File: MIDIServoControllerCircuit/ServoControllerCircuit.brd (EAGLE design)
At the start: 59 x 66 mm, 26 parts, among them Q1 20MHz, T1 2N3904, X1 SIGNAL-PWR-GND, X2 SIGNAL-PWR-GND

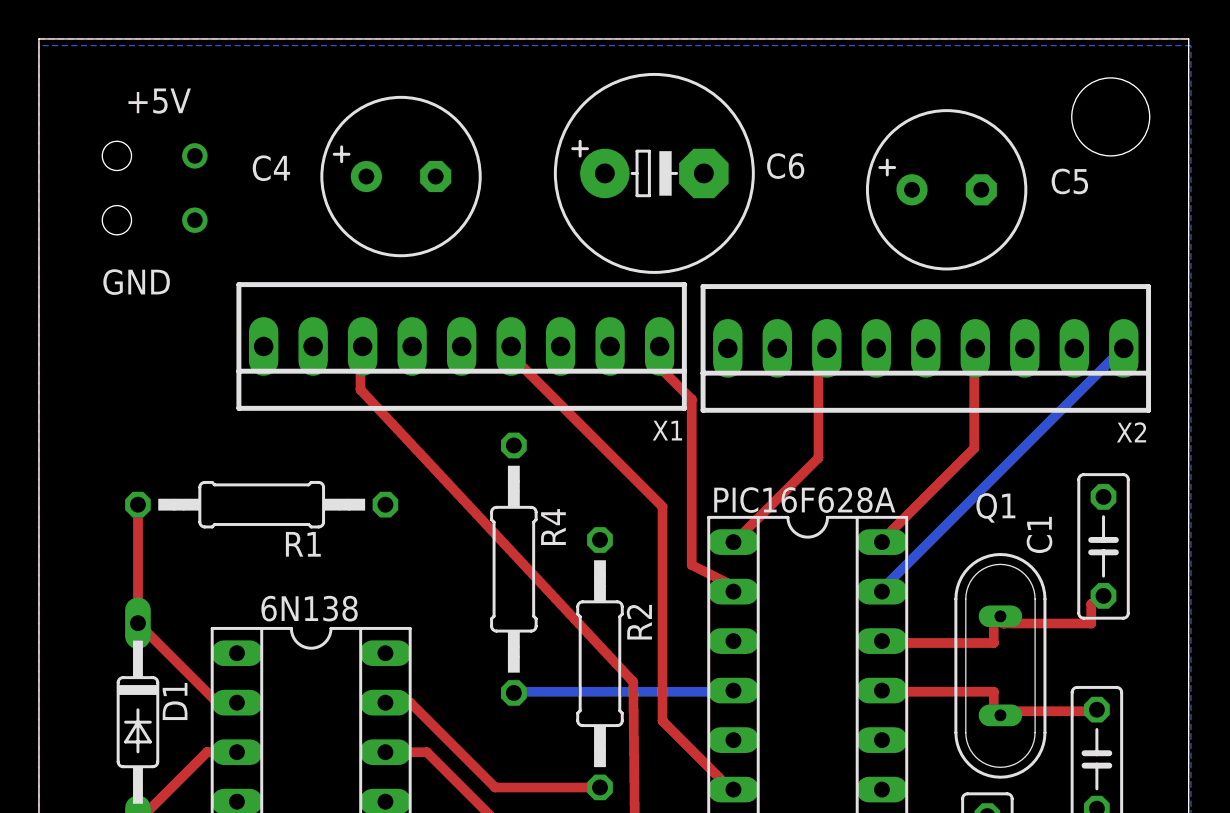
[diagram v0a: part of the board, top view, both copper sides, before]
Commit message: Added Servo Labels to Board Layout
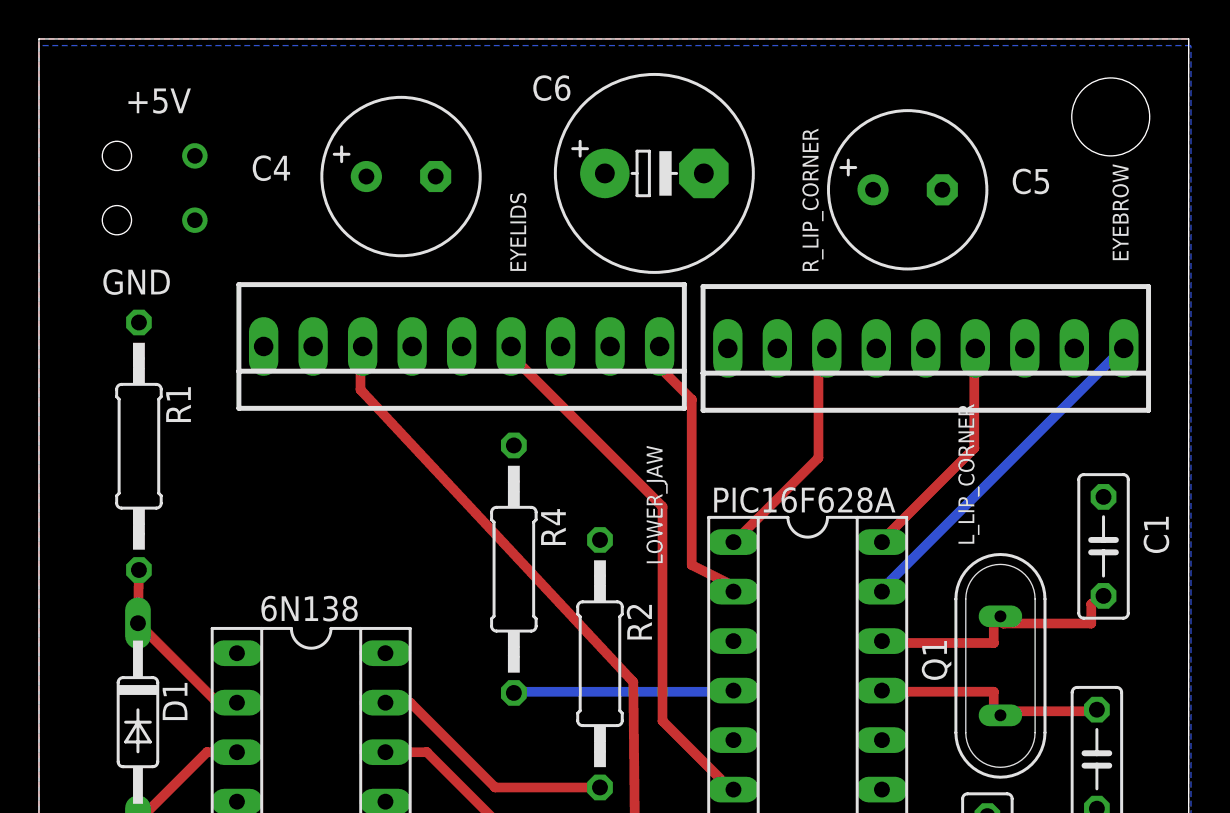
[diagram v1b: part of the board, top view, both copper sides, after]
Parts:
- moved R1 6.98 mm to (5.13, 45.1), turned to 270 degrees
- moved C5 2.00 mm to (44.6, 58.3)
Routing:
- net N$1: track 12.8 -> 9.50 mm
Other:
- board text added: "EYEBROW"
- board text added: "EYELIDS"
- board text added: "LOWER_JAW"
- board text added: "L_LIP_CORNER"
- board text added: "R_LIP_CORNER"
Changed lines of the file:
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@@
 <hole x="4" y="4" drill="4"/>
 <hole x="55" y="62" drill="4"/>
+<text x="55.1" y="59.6" size="0.8128" layer="21" rot="R270">EYEBROW</text>
+<text x="48" y="40" size="0.8128" layer="21" rot="R90">L_LIP_CORNER</text>
+<text x="40" y="54" size="0.8128" layer="21" rot="R90">R_LIP_CORNER</text>
+<text x="32" y="39" size="0.8128" layer="21" rot="R90">LOWER_JAW</text>
+<text x="25" y="54" size="0.8128" layer="21" rot="R90">EYELIDS</text>
 </plain>
 <attributes>
@@
 </element>
 <element name="C1" library="resistor" library_urn="urn:adsk.eagle:library:348" package="C050-025X075" package3d_urn="urn:adsk.eagle:package:26160/1" value="22p" x="54.63" y="39.96" smashed="yes" rot="R90">
-<attribute name="NAME" x="51.979" y="39.531" size="1.27" layer="25" ratio="10" rot="R90"/>
+<attribute name="NAME" x="57.979" y="39.531" size="1.27" layer="25" ratio="10" rot="R90"/>
 </element>
 <element name="C2" library="resistor" library_urn="urn:adsk.eagle:library:348" package="C050-025X075" package3d_urn="urn:adsk.eagle:package:26160/1" value="22p" x="54.29" y="29.04" smashed="yes" rot="R270">
@@
 <attribute name="NAME" x="10.882" y="58.734" size="1.27" layer="25" ratio="10"/>
 </element>
-<element name="C5" library="resistor" library_urn="urn:adsk.eagle:library:348" package="E3,5-8" package3d_urn="urn:adsk.eagle:package:25842/1" value="330uF" x="46.58" y="58.26" smashed="yes">
-<attribute name="NAME" x="51.882" y="58.054" size="1.27" layer="25" ratio="10"/>
+<element name="C5" library="resistor" library_urn="urn:adsk.eagle:library:348" package="E3,5-8" package3d_urn="urn:adsk.eagle:package:25842/1" value="330uF" x="44.58" y="58.26" smashed="yes">
+<attribute name="NAME" x="49.882" y="58.054" size="1.27" layer="25" ratio="10"/>
 </element>
 <element name="C6" library="resistor" library_urn="urn:adsk.eagle:library:348" package="E5-10,5" package3d_urn="urn:adsk.eagle:package:25854/1" value="1000uF" x="31.58" y="59.1" smashed="yes">
-<attribute name="NAME" x="37.279" y="58.8432" size="1.27" layer="25" ratio="10"/>
+<attribute name="NAME" x="25.279" y="62.8432" size="1.27" layer="25" ratio="10"/>
 </element>
 <element name="D1" library="diode" library_urn="urn:adsk.eagle:library:210" package="DO35-10" package3d_urn="urn:adsk.eagle:package:43344/2" value="1N4148" x="5.08" y="30.94" smashed="yes" rot="R270">
@@
 <element name="PIC16F628A" library="ic-package" library_urn="urn:adsk.eagle:library:239" package="SOCKET-18" package3d_urn="urn:adsk.eagle:package:14434/1" value="" x="39.45" y="30.02" rot="R270"/>
 <element name="Q1" library="special" library_urn="urn:adsk.eagle:library:367" package="QS" package3d_urn="urn:adsk.eagle:package:26647/2" value="20MHz" x="49.34" y="33.83" smashed="yes" rot="R90">
-<attribute name="NAME" x="50.25" y="42.673" size="1.27" layer="25" ratio="10" rot="R180"/>
-</element>
-<element name="R1" library="resistor" library_urn="urn:adsk.eagle:library:348" package="0207/12" package3d_urn="urn:adsk.eagle:package:25938/1" value="220" x="11.43" y="42.1" smashed="yes" rot="R180">
-<attribute name="NAME" x="14.605" y="40.703" size="1.27" layer="25" ratio="10" rot="R180"/>
+<attribute name="NAME" x="45.327" y="35.25" size="1.27" layer="25" ratio="10" rot="R270"/>
+</element>
+<element name="R1" library="resistor" library_urn="urn:adsk.eagle:library:348" package="0207/12" package3d_urn="urn:adsk.eagle:package:25938/1" value="220" x="5.13" y="45.1" smashed="yes" rot="R270">
+<attribute name="NAME" x="6.527" y="48.275" size="1.27" layer="25" ratio="10" rot="R270"/>
 </element>
 <element name="R2" library="resistor" library_urn="urn:adsk.eagle:library:348" package="0207/12" package3d_urn="urn:adsk.eagle:package:25938/1" value="4.7k" x="28.79" y="33.94" smashed="yes" rot="R270">
@@
 <attribute name="MF" value="MOLEX" x="21.69" y="50.22" size="1.778" layer="27" rot="R180" display="off"/>
 <attribute name="MPN" value="22-23-2091" x="21.69" y="50.22" size="1.778" layer="27" rot="R180" display="off"/>
-<attribute name="NAME" x="33.12" y="46.41" size="1.016" layer="25" ratio="10" rot="R180"/>
 <attribute name="OC_FARNELL" value="1756827" x="21.69" y="50.22" size="1.778" layer="27" rot="R180" display="off"/>
 <attribute name="OC_NEWARK" value="56H0450" x="21.69" y="50.22" size="1.778" layer="27" rot="R180" display="off"/>
@@
 <attribute name="MF" value="MOLEX" x="45.51" y="50.12" size="1.778" layer="27" rot="R180" display="off"/>
 <attribute name="MPN" value="22-23-2091" x="45.51" y="50.12" size="1.778" layer="27" rot="R180" display="off"/>
-<attribute name="NAME" x="56.94" y="46.31" size="1.016" layer="25" ratio="10" rot="R180"/>
 <attribute name="OC_FARNELL" value="1756827" x="45.51" y="50.12" size="1.778" layer="27" rot="R180" display="off"/>
 <attribute name="OC_NEWARK" value="56H0450" x="45.51" y="50.12" size="1.778" layer="27" rot="R180" display="off"/>
@@
 <contactref element="D1" pad="C"/>
 <contactref element="R1" pad="2"/>
-<wire x1="5.08" y1="36.02" x2="5.08" y2="42.1" width="0.5" layer="1"/>
+<wire x1="5.08" y1="36.02" x2="5.13" y2="38.75" width="0.5" layer="1"/>
 <wire x1="5.08" y1="36.02" x2="9.16" y2="31.94" width="0.5" layer="1"/>
 <wire x1="9.16" y1="31.94" x2="10.16" y2="31.94" width="0.5" layer="1"/>

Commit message: Updated Circuit for better PIC to compensate for more motor control.
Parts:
- removed 6N138: (no value), ic-package:SOCKET-08
- removed C1, C2: 22p, resistor:C050-025X075
- removed PIC16F628A: (no value), ic-package:SOCKET-18
- removed Q1: 20MHz, special:QS
- removed R4: 10k, resistor:0207/12
- added MIDI_OUT_PIN-2, MIDI_OUT_PIN-4, MIDI_OUT_PIN-5: DOUBLE_THROUGH_HOLE_PAD, DOUBLE_THROUGH_HOLE_PAD:DOUBLE_THROUGH_HOLE_PAD
- added OK1: 6N138, optocoupler:DIL08
- added R8, R9: 220, resistor:0207/12
- added U$1: PIC18F24K40-I/SP, Microchip_By_element14_Batch_1:DIP254P762X508-28
- renumbered MIDI_PIN-4 to MIDI_IN_PIN-4, MIDI_PIN-5 to MIDI_IN_PIN-5
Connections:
- removed net LOWER_JAR: PIC16F628A.2, X1.1
- removed net N$3: C1.1, PIC16F628A.16, Q1.2
- removed net N$4: C2.1, PIC16F628A.15, Q1.1
- removed net N$6: PIC16F628A.4, R4.2
- new net LOWER_JAW: U$1.5, X1.1
- new net N$11: MIDI_OUT_PIN-4.P$1, R8.1
- new net TX_PIN: R9.2, U$1.17
- net +5V: now also OK1.8, R8.2, U$1.20; no longer 6N138.8, PIC16F628A.14, R4.1
- net EYEBROW: now also U$1.2; no longer PIC16F628A.17
- net EYELIDS: now also U$1.6; no longer PIC16F628A.6
- net GND: now also MIDI_OUT_PIN-2.P$1, MIDI_OUT_PIN-5.P$1, OK1.5, R9.1, U$1.19, U$1.8; no longer 6N138.5, C1.2, C2.2, PIC16F628A.5
- net LEFT_LIP_CORNER: now also U$1.3; no longer PIC16F628A.18
- net LIGHTS: now also U$1.9; no longer PIC16F628A.11
- net MIDI_PIN-5: now also OK1.3; no longer 6N138.3
- net N$1: now also OK1.2; no longer 6N138.2
- net N$2: now also OK1.7; no longer 6N138.7
- net RIGHT_LIP_CORNER: now also U$1.4; no longer PIC16F628A.1
- net RX_PIN: now also OK1.6, U$1.18; no longer 6N138.6, PIC16F628A.7
- net UNUSED: now also U$1.7; no longer PIC16F628A.9
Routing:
- net LOWER_JAR: track 14.5 -> 0.00 mm
- net LOWER_JAW: track 0.00 -> 14.1 mm
- net N$3: track 13.9 -> 0.00 mm
- net N$4: track 12.2 -> 0.00 mm
- net N$6: track 11.3 -> 0.00 mm
- net RX_PIN: track 24.9 -> 22.3 mm
- net MIDI_PIN-5: track 10.5 -> 8.94 mm
- net N$2: track 12.8 -> 11.5 mm
- net N$1: track 9.50 -> 8.50 mm
- net LIGHTS: track 13.0 -> 12.2 mm

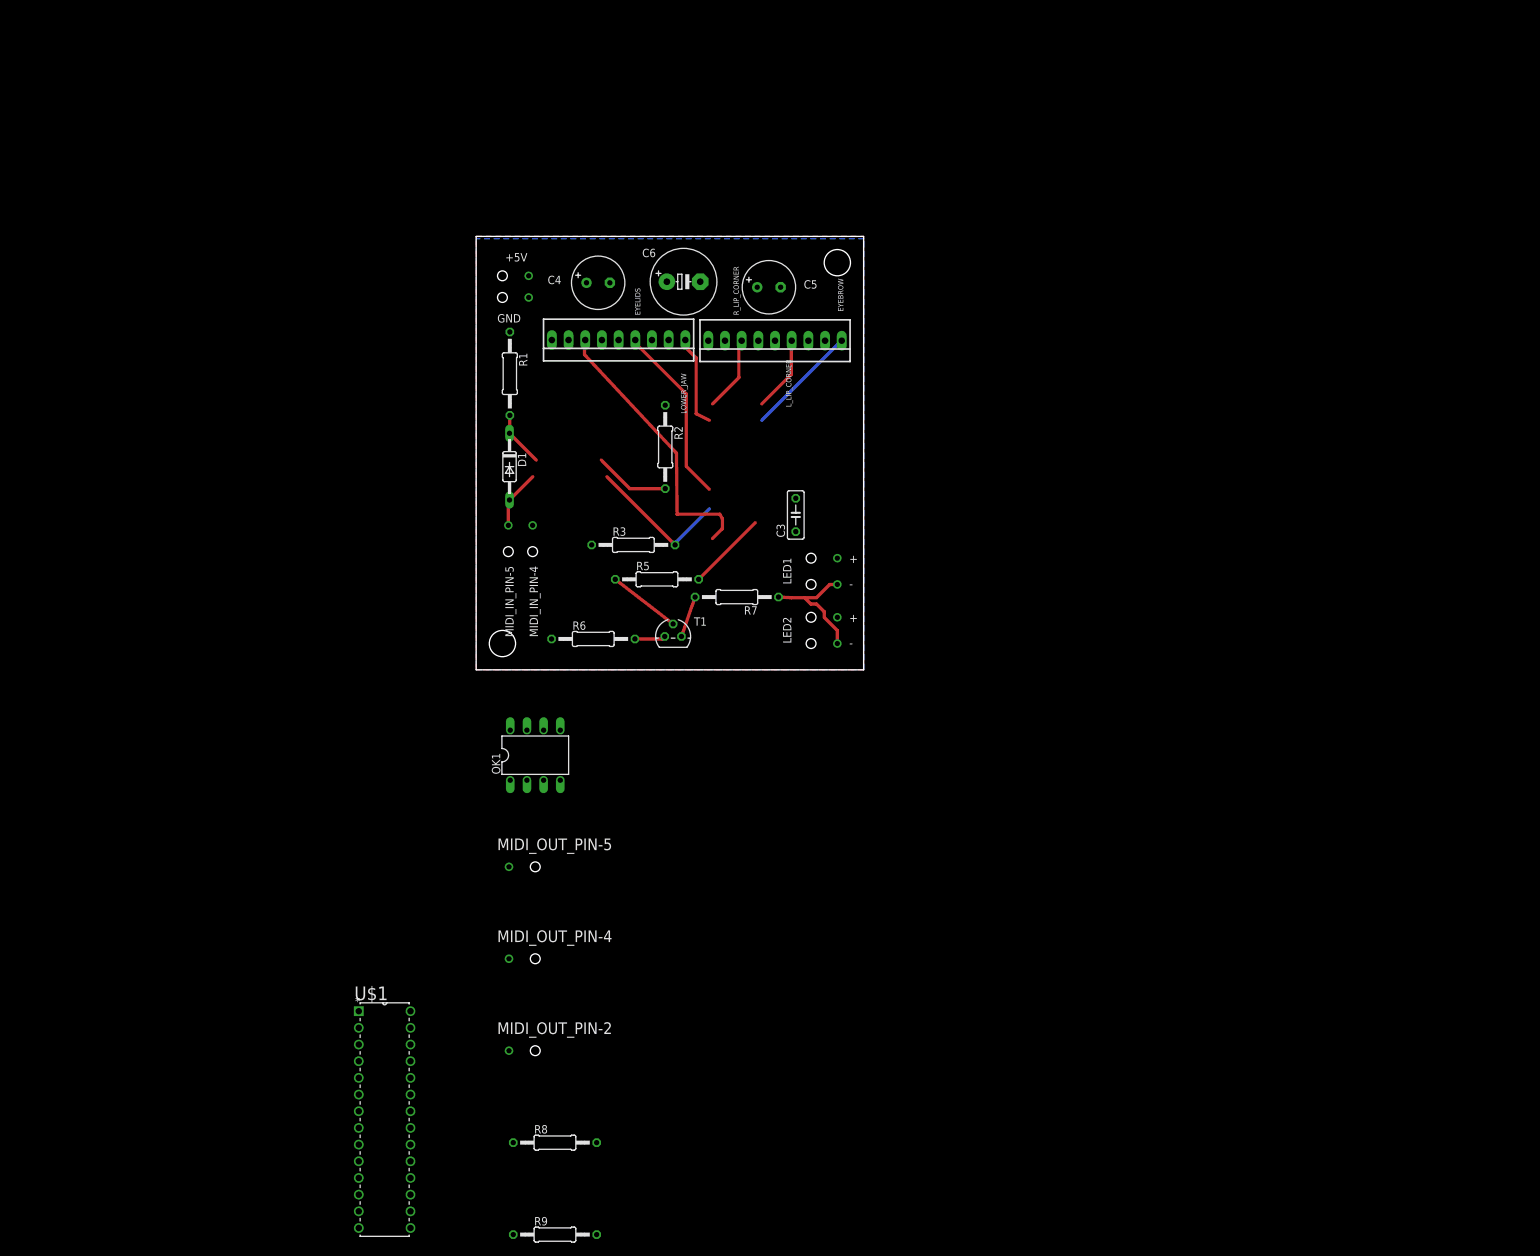
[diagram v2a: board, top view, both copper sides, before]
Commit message: Took MIDI output and input circuits out, replaced with XBee circuit. Cleaned up schematic.
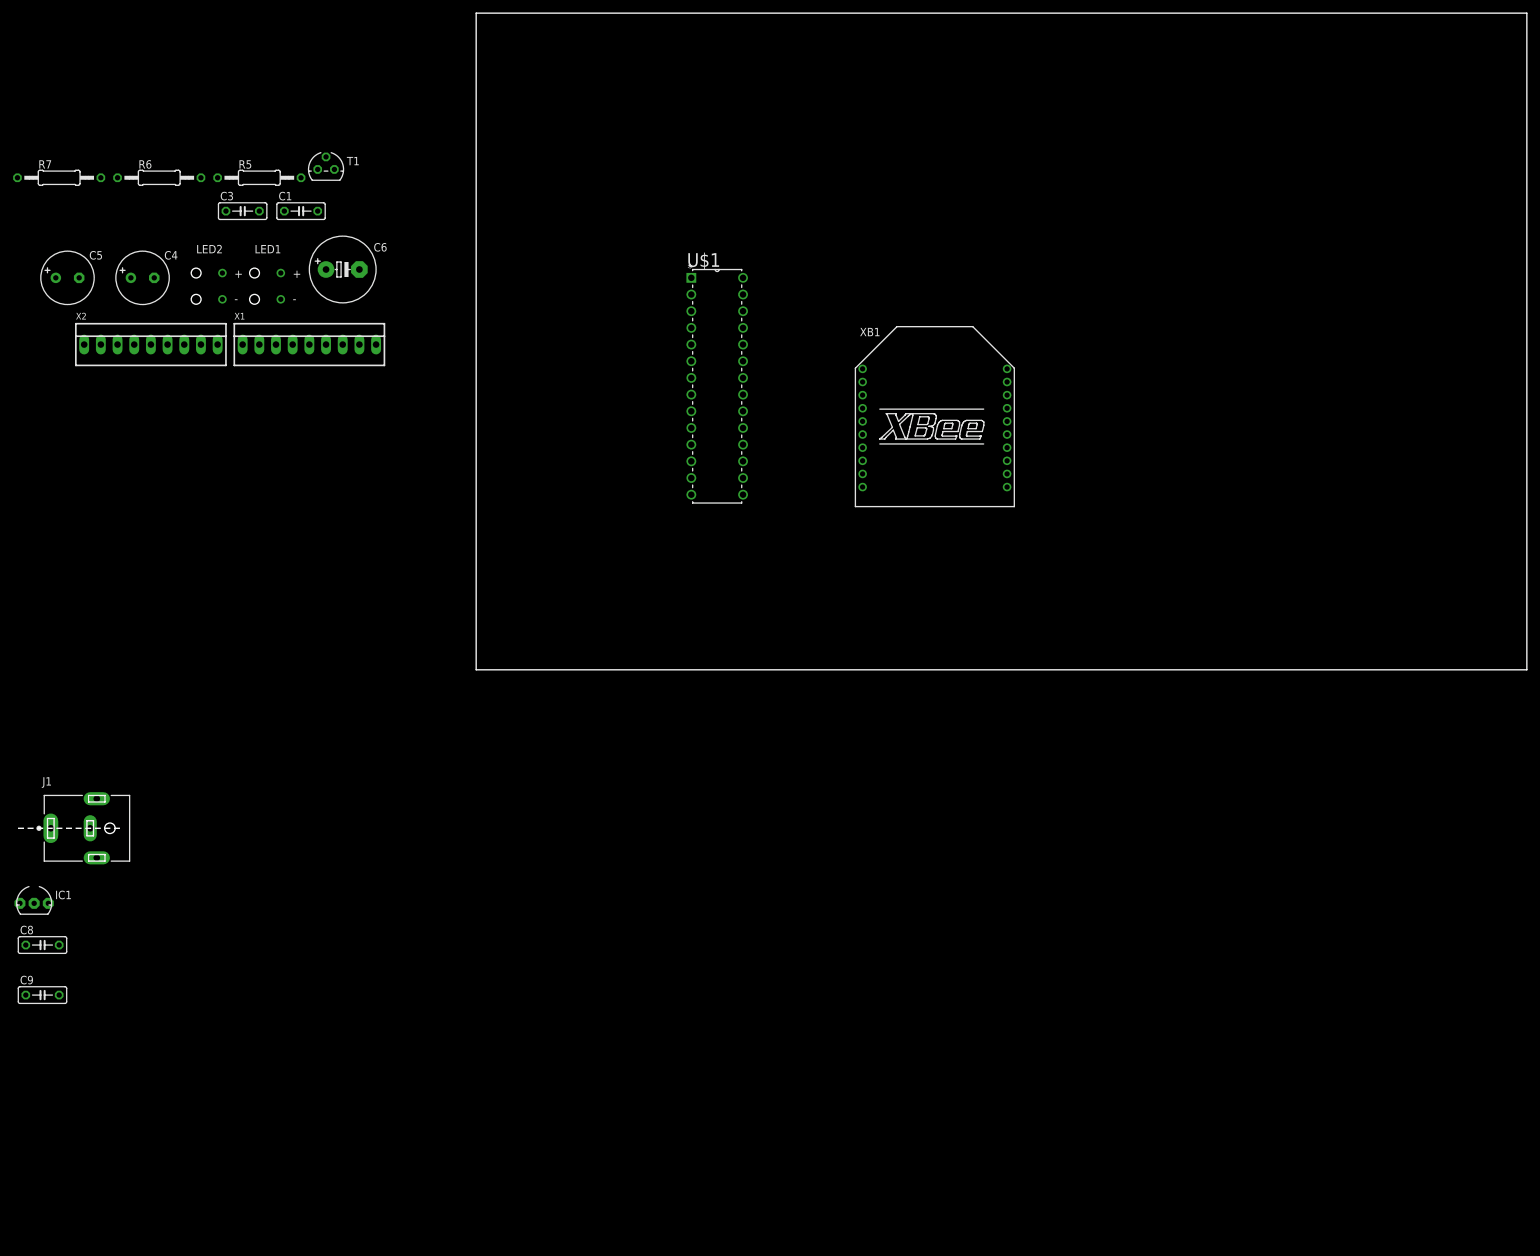
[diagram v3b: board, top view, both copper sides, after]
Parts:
- removed +5V, GND, MIDI_IN_PIN-4, MIDI_IN_PIN-5, MIDI_OUT_PIN-2, MIDI_OUT_PIN-4, MIDI_OUT_PIN-5: DOUBLE_THROUGH_HOLE_PAD, DOUBLE_THROUGH_HOLE_PAD:DOUBLE_THROUGH_HOLE_PAD
- removed D1: 1N4148, diode:DO35-10
- removed OK1: 6N138, optocoupler:DIL08
- removed R1, R8, R9: 220, resistor:0207/12
- removed R2: 4.7k, resistor:0207/12
- removed R3: 270, resistor:0207/12
- added C1: 0.1u, resistor:C050-025X075
- added C8, C9: 1u, resistor:C050-025X075
- added IC1: MCP1700INLINE, MCP1700:TO92-INLINE
- added J1: PJ-063BH, PJ-063BH:CUI_PJ-063BH
- added XB1: XBEE, maxstream:XBEE
- moved U$1 122.6 mm to (40.6, 26.7)
- moved R7 121.3 mm to (-63.5, 74.9), turned to 0 degrees
- moved LED2 107.3 mm to (-40.6, 58.4)
- moved C5 106.8 mm to (-62.2, 59.7)
- moved R6 96.4 mm to (-48.3, 74.9)
- moved C3 96.1 mm to (-35.6, 69.8), turned to 0 degrees
- moved LED1 95.2 mm to (-31.8, 58.4)
- moved X2 95.0 mm to (-49.5, 49.5), turned to 0 degrees
- moved T1 88.6 mm to (-22.9, 76.2)
- moved R5 86.1 mm to (-33.0, 74.9)
- moved C4 69.4 mm to (-50.8, 59.7)
- moved C6 51.9 mm to (-20.3, 61.0)
- moved X1 47.1 mm to (-25.4, 49.5), turned to 0 degrees
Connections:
- removed net MIDI_PIN-5: D1.A, MIDI_IN_PIN-5.P$1, OK1.3
- removed net N$1: D1.C, OK1.2, R1.2
- removed net N$11: MIDI_OUT_PIN-4.P$1, R8.1
- removed net N$2: OK1.7, R2.2
- removed net RX_PIN: OK1.6, R3.2, U$1.18
- removed net TX_PIN: R9.2, U$1.17
- new net +3.3V: C1.1, C8.2, IC1.3, XB1.1
- new net PIC_RX: U$1.18, XB1.2
- new net PIC_TX: U$1.17, XB1.3
- new net SHIELD: J1.S1, J1.S2
- net +5V: now also C9.1, IC1.2, J1.1; no longer +5V.P$1, OK1.8, R3.1, R8.2
- net GND: now also C1.2, C8.1, C9.2, IC1.1, J1.2, XB1.10; no longer GND.P$1, MIDI_IN_PIN-4.P$1, MIDI_OUT_PIN-2.P$1, MIDI_OUT_PIN-5.P$1, OK1.5, R1.1, R2.1, R9.1
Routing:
- net UNUSED: track 43.0 -> 0.00 mm
- net EYELIDS: track 27.4 -> 0.00 mm
- net RX_PIN: track 22.3 -> 0.00 mm
- net N$10: track 19.4 -> 0.00 mm
- net EYEBROW: track 17.2 -> 0.00 mm
- net LOWER_JAW: track 14.1 -> 0.00 mm
- net LIGHTS: track 12.2 -> 0.00 mm
- net RIGHT_LIP_CORNER: track 11.6 -> 0.00 mm
- net N$2: track 11.5 -> 0.00 mm
- net LEFT_LIP_CORNER: track 11.5 -> 0.00 mm
- net N$5: track 11.1 -> 0.00 mm
- net MIDI_PIN-5: track 8.94 -> 0.00 mm
- net N$1: track 8.50 -> 0.00 mm
- net N$9: track 6.35 -> 0.00 mm
- net N$7: track 4.70 -> 0.00 mm
- removed copper zone on layer 1, net +5V
- removed copper zone on layer 16, net GND
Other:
- board size 59 x 66 mm -> 160 x 100 mm
- board text removed: "EYEBROW"
- board text removed: "EYELIDS"
- board text removed: "LOWER_JAW"
- board text removed: "L_LIP_CORNER"
- board text removed: "R_LIP_CORNER"
